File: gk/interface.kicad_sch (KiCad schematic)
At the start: 63 parts, among them J11 Conn_01x02, SW3 RotaryEncoder_Switch, U9 LSM6DSL

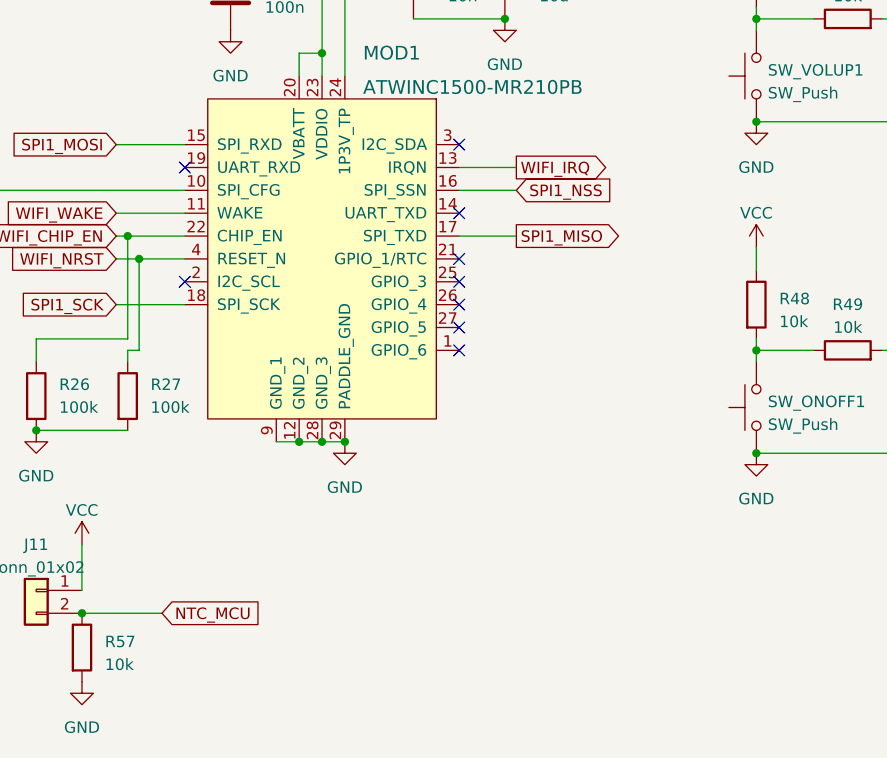
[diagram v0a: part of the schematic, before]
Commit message: Add winc uart programming header
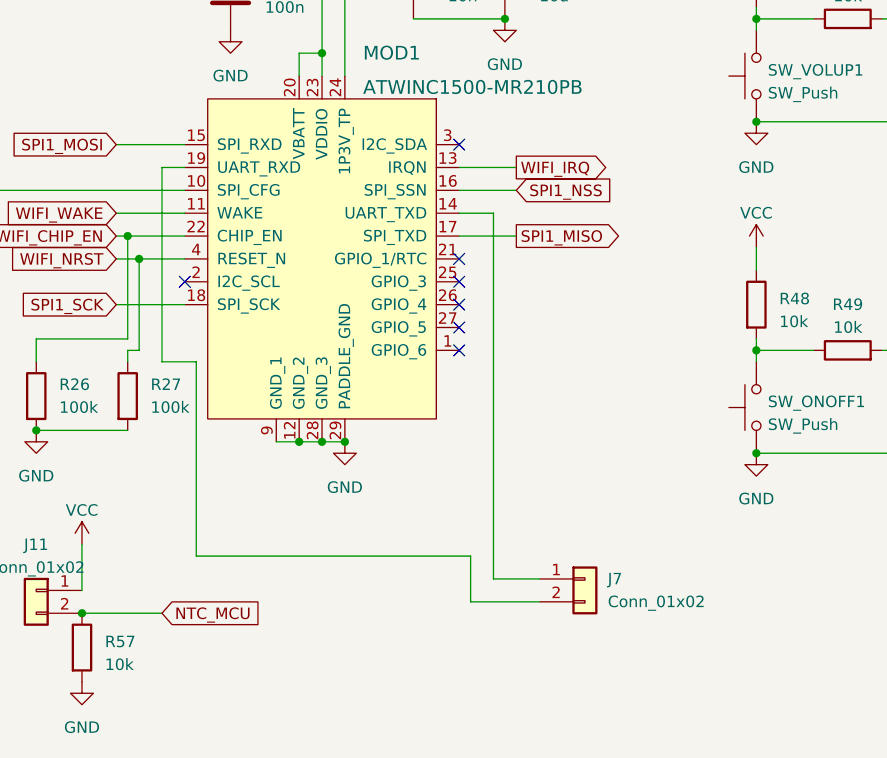
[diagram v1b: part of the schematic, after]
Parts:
- added J7: Conn_01x02, Connector_PinHeader_2.54mm:PinHeader_1x02_P2.54mm_Vertical, symbol Connector_Generic:Conn_01x02
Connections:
- net at MOD1.14 (UART_TXD): now also J7.1 (Pin_1)
- net at MOD1.19 (UART_RXD): now also J7.2 (Pin_2)
- no-connect marks 10 -> 8
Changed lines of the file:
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@@
   (no_connect (at 96.52 149.86))
   (no_connect (at 96.52 147.32))
-  (no_connect (at 96.52 137.16))
-  (no_connect (at 66.04 132.08))
   (no_connect (at 96.52 129.54))
   (no_connect (at 96.52 142.24))
@@
     (stroke (width 0) (type default))
   )
+  (wire (pts (xy 97.79 180.34) (xy 105.41 180.34))
+    (stroke (width 0) (type default))
+  )
   (wire (pts (xy 198.12 77.47) (xy 198.12 78.74))
     (stroke (width 0) (type default))
@@
     (stroke (width 0) (type default))
   )
+  (wire (pts (xy 67.31 175.26) (xy 97.79 175.26))
+    (stroke (width 0) (type default))
+  )
   (wire (pts (xy 232.41 66.04) (xy 232.41 68.58))
     (stroke (width 0) (type default))
@@
     (stroke (width 0) (type default))
   )
+  (wire (pts (xy 63.5 153.67) (xy 67.31 153.67))
+    (stroke (width 0) (type default))
+  )
   (wire (pts (xy 232.41 115.57) (xy 232.41 116.84))
     (stroke (width 0) (type default))
@@
     (stroke (width 0) (type default))
   )
+  (wire (pts (xy 96.52 137.16) (xy 100.33 137.16))
+    (stroke (width 0) (type default))
+  )
   (wire (pts (xy 29.21 66.04) (xy 33.02 66.04))
     (stroke (width 0) (type default))
@@
     (stroke (width 0) (type default))
   )
+  (wire (pts (xy 63.5 132.08) (xy 63.5 153.67))
+    (stroke (width 0) (type default))
+  )
   (wire (pts (xy 186.69 115.57) (xy 190.5 115.57))
     (stroke (width 0) (type default))
@@
     (stroke (width 0) (type default))
   )
+  (wire (pts (xy 66.04 132.08) (xy 63.5 132.08))
+    (stroke (width 0) (type default))
+  )
   (wire (pts (xy 58.42 38.1) (xy 58.42 39.37))
     (stroke (width 0) (type default))
@@
     (stroke (width 0) (type default))
   )
+  (wire (pts (xy 100.33 177.8) (xy 105.41 177.8))
+    (stroke (width 0) (type default))
+  )
   (wire (pts (xy 232.41 50.8) (xy 250.19 50.8))
     (stroke (width 0) (type default))
@@
     (stroke (width 0) (type default))
   )
+  (wire (pts (xy 97.79 175.26) (xy 97.79 180.34))
+    (stroke (width 0) (type default))
+  )
   (wire (pts (xy 232.41 127) (xy 250.19 127))
     (stroke (width 0) (type default))
@@
   )
   (wire (pts (xy 129.54 127) (xy 147.32 127))
+    (stroke (width 0) (type default))
+  )
+  (wire (pts (xy 67.31 153.67) (xy 67.31 175.26))
+    (stroke (width 0) (type default))
+  )
+  (wire (pts (xy 100.33 137.16) (xy 100.33 177.8))
     (stroke (width 0) (type default))
   )
@@
         )
       )
+    )
+  )
+  (symbol (lib_id "Connector_Generic:Conn_01x02") (at 110.49 177.8 0) (unit 1)
+    (in_bom yes) (on_board yes) (dnp no) (fields_autoplaced)
+    (property "Reference" "J7" (at 113.03 177.8 0)
+      (effects (font (size 1.27 1.27)) (justify left))
+    )
+    (property "Value" "Conn_01x02" (at 113.03 180.34 0)
+      (effects (font (size 1.27 1.27)) (justify left))
+    )
+    (property "Footprint" "Connector_PinHeader_2.54mm:PinHeader_1x02_P2.54mm_Vertical" (at 110.49 177.8 0)
+      (effects (font (size 1.27 1.27)) hide)
+    )
+    (property "Datasheet" "~" (at 110.49 177.8 0)
+      (effects (font (size 1.27 1.27)) hide)
+    )
+    (pin "1")
+    (pin "2")
+    (instances
+      (project "gk"
+        (path "/08730ac6-6084-459f-bdf1-86b322355ede/fa96f0b5-5dfb-45a6-bb43-c2cb84c619a5"
+          (reference "J7") (unit 1)
+        )
+      )

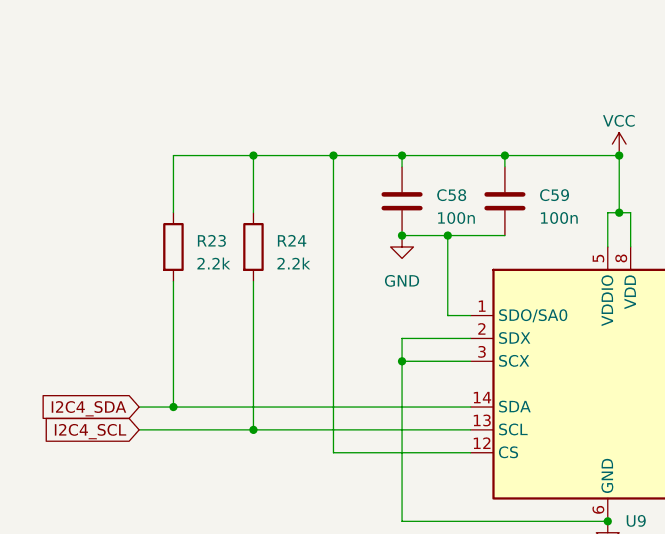
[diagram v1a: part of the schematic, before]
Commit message: i2c resistor calculations
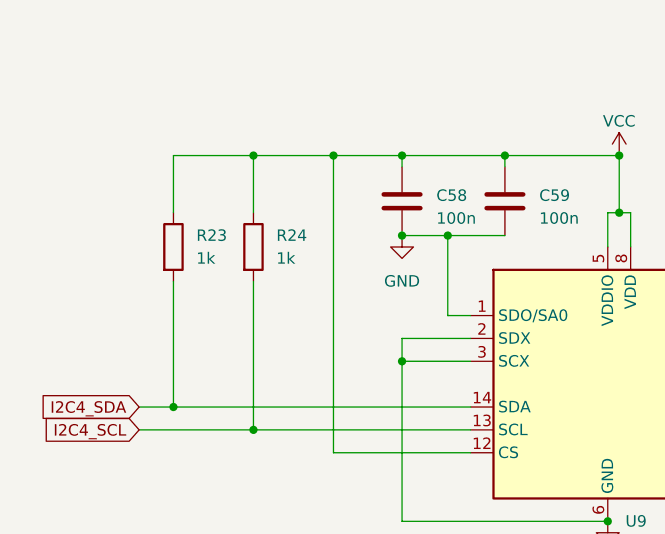
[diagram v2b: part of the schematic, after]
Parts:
- R23, R24: value 2.2k -> 1k
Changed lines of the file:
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@@
   (symbol (lib_id "Device:R") (at 41.91 48.26 0) (unit 1)
     (in_bom yes) (on_board yes) (dnp no) (fields_autoplaced)
-    (property "Reference" "R24" (at 44.45 47.625 0)
-      (effects (font (size 1.27 1.27)) (justify left))
-    )
-    (property "Value" "2.2k" (at 44.45 50.165 0)
+    (property "Reference" "R24" (at 44.45 46.99 0)
+      (effects (font (size 1.27 1.27)) (justify left))
+    )
+    (property "Value" "1k" (at 44.45 49.53 0)
       (effects (font (size 1.27 1.27)) (justify left))
     )
@@
   (symbol (lib_id "Device:R") (at 33.02 48.26 0) (unit 1)
     (in_bom yes) (on_board yes) (dnp no) (fields_autoplaced)
-    (property "Reference" "R23" (at 35.56 47.625 0)
-      (effects (font (size 1.27 1.27)) (justify left))
-    )
-    (property "Value" "2.2k" (at 35.56 50.165 0)
-      (effects (font (size 1.27 1.27)) (justify left))
-    )
+    (property "Reference" "R23" (at 35.56 46.99 0)
+      (effects (font (size 1.27 1.27)) (justify left))
+    )
+    (property "Value" "1k" (at 35.56 49.53 0)
+      (effects (font (size 1.27 1.27)) (justify left))
+    )
